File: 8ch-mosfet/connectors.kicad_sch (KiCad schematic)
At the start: 10 parts, among them J1 N2K, J2 I2C

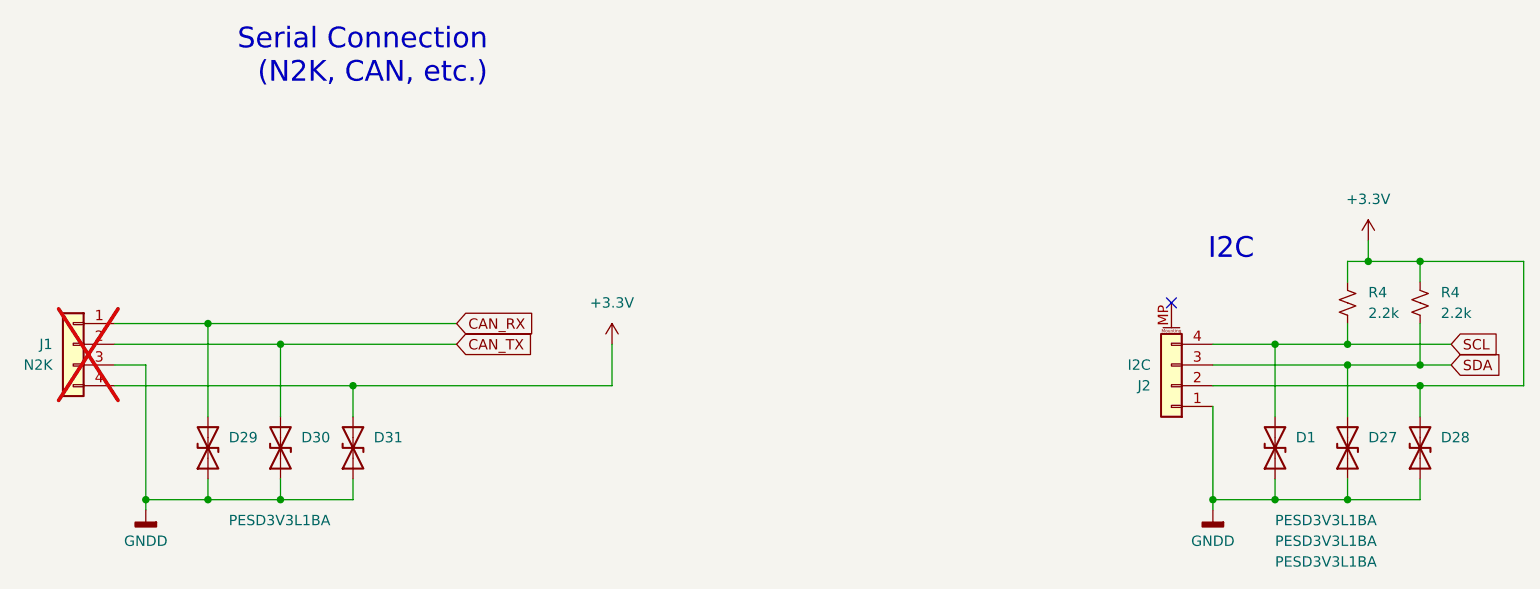
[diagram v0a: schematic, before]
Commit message: changed to MCP3564
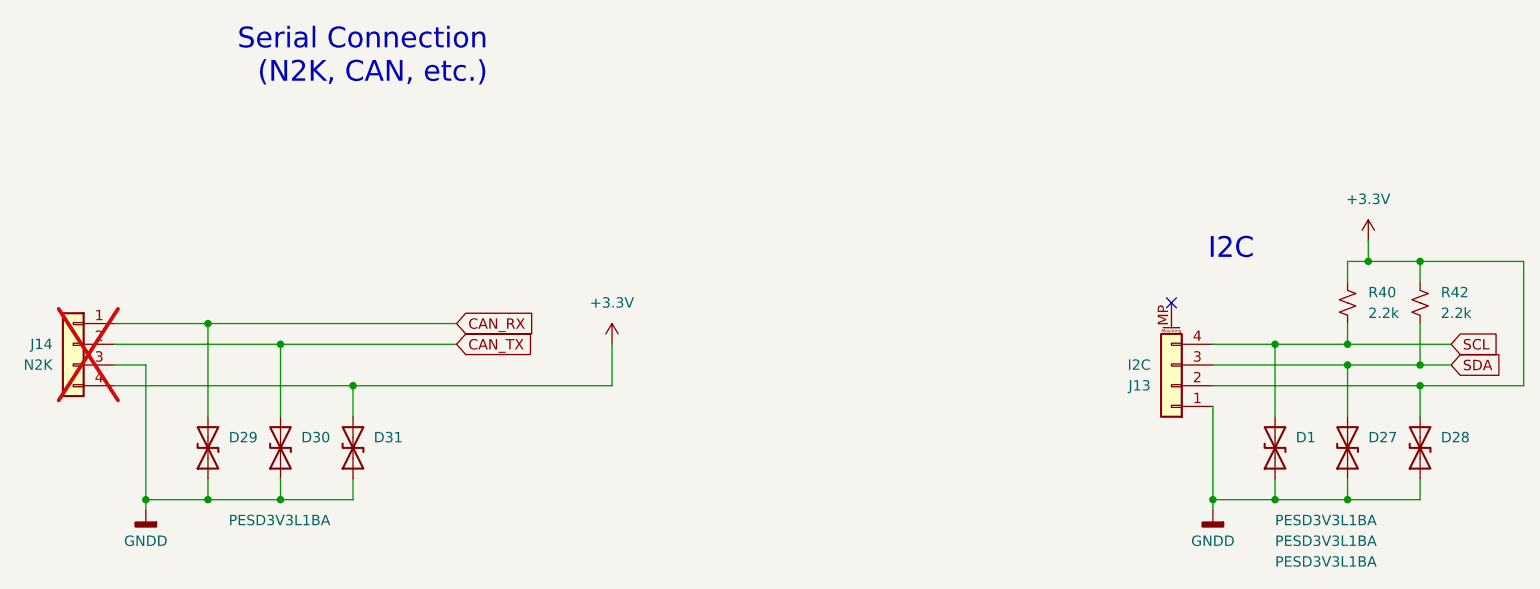
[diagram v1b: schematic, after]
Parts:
- renumbered J2 to J13, J1 to J14, R4 to R40, R4 to R42

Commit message: big update - 12ch, volt adc, senders, etc.
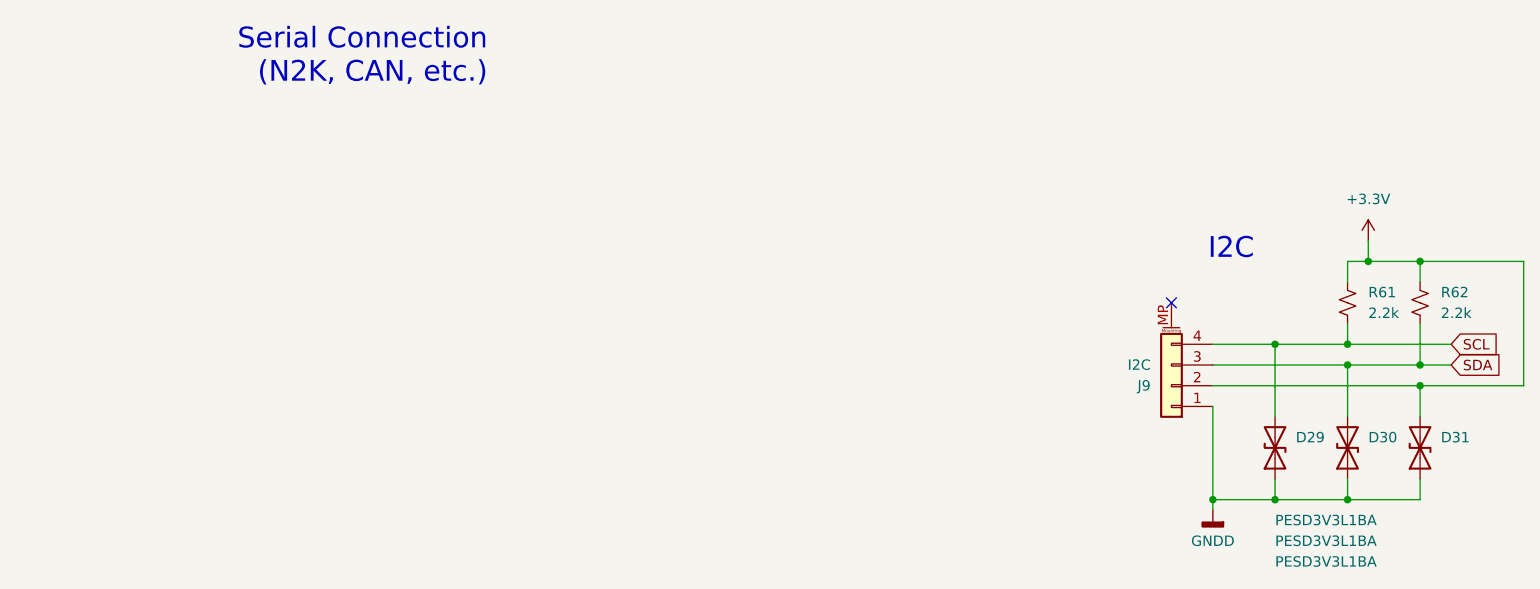
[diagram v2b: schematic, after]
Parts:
- removed D29, D30, D31: PESD3V3L1BA, Diode_SMD:D_SOD-323_HandSoldering, symbol Device:D_TVS
- removed J14: N2K, Connector_PinHeader_2.54mm:PinHeader_1x04_P2.54mm_Vertical, symbol Connector_Generic:Conn_01x04
- renumbered D1 to D29, D27 to D30, D28 to D31, J13 to J9, R40 to R61, R42 to R62

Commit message: component layout looking crispy.
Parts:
- removed D29, D30, D31: PESD3V3L1BA, Diode_SMD:D_SOD-323_HandSoldering, symbol Device:D_TVS
- removed J9: I2C, Connector_JST:JST_SH_SM04B-SRSS-TB_1x04-1MP_P1.00mm_Horizontal, symbol Connector_Generic_MountingPin:Conn_01x04_MountingPin
- removed R61, R62: 2.2k, Resistor_SMD:R_0805_2012Metric_Pad1.20x1.40mm_HandSolder, symbol Device:R_Small_US
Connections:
- no-connect marks 1 -> 0
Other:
- note removed: "I2C"
